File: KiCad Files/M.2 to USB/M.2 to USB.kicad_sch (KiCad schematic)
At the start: 32 parts, among them J1 M.2 A+E Key Connector, J2 Conn_2Rows-09Pins_ALT, U1 USB2422T_MJ, U2 AP2152SG-13, U3 MIC2876-5.0, U4 SN74LVC1G14DBVR, Y1 OSC24M-3.3I/S3

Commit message: New Renders and updated board
updated the footprints for usb2422, clock chip and m.2 connector.

made new 2D and 3D renders of updated board.
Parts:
- J1: now left out of the parts list
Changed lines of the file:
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@@
 		(unit 1)
 		(exclude_from_sim no)
-		(in_bom yes)
+		(in_bom no)
 		(on_board yes)
 		(dnp no)

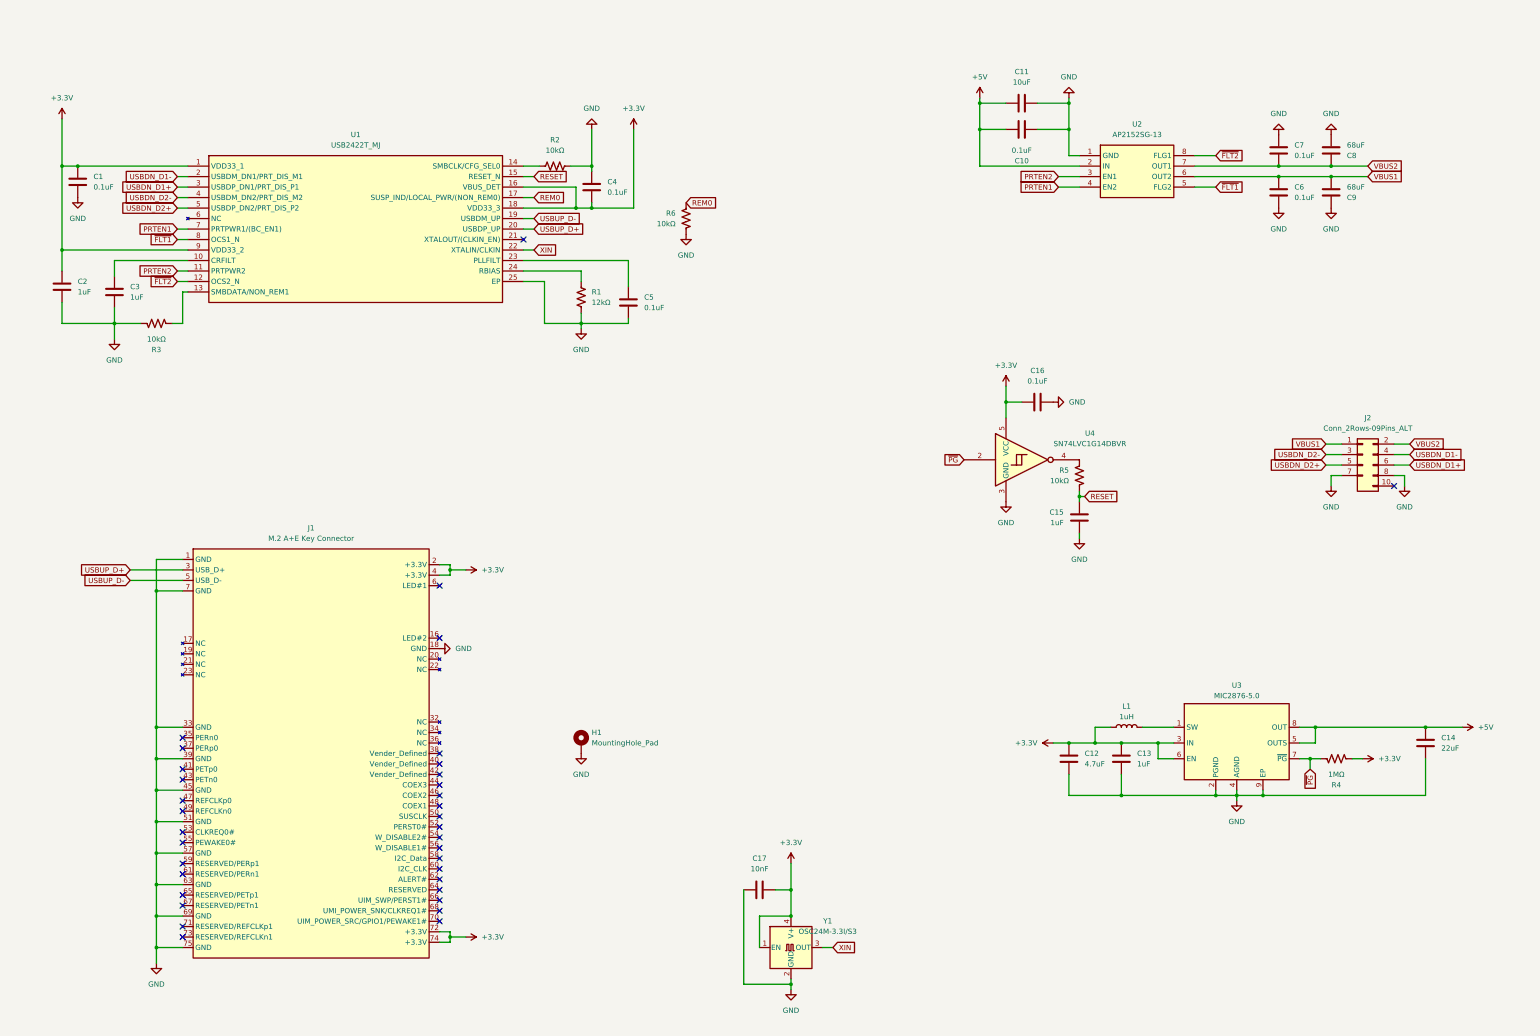
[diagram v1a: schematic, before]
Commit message: Updated v1.1 design
-updated v1.1 design
-finished schematic, pcb, render, gerber, and BOM
-removed old v1.0 files
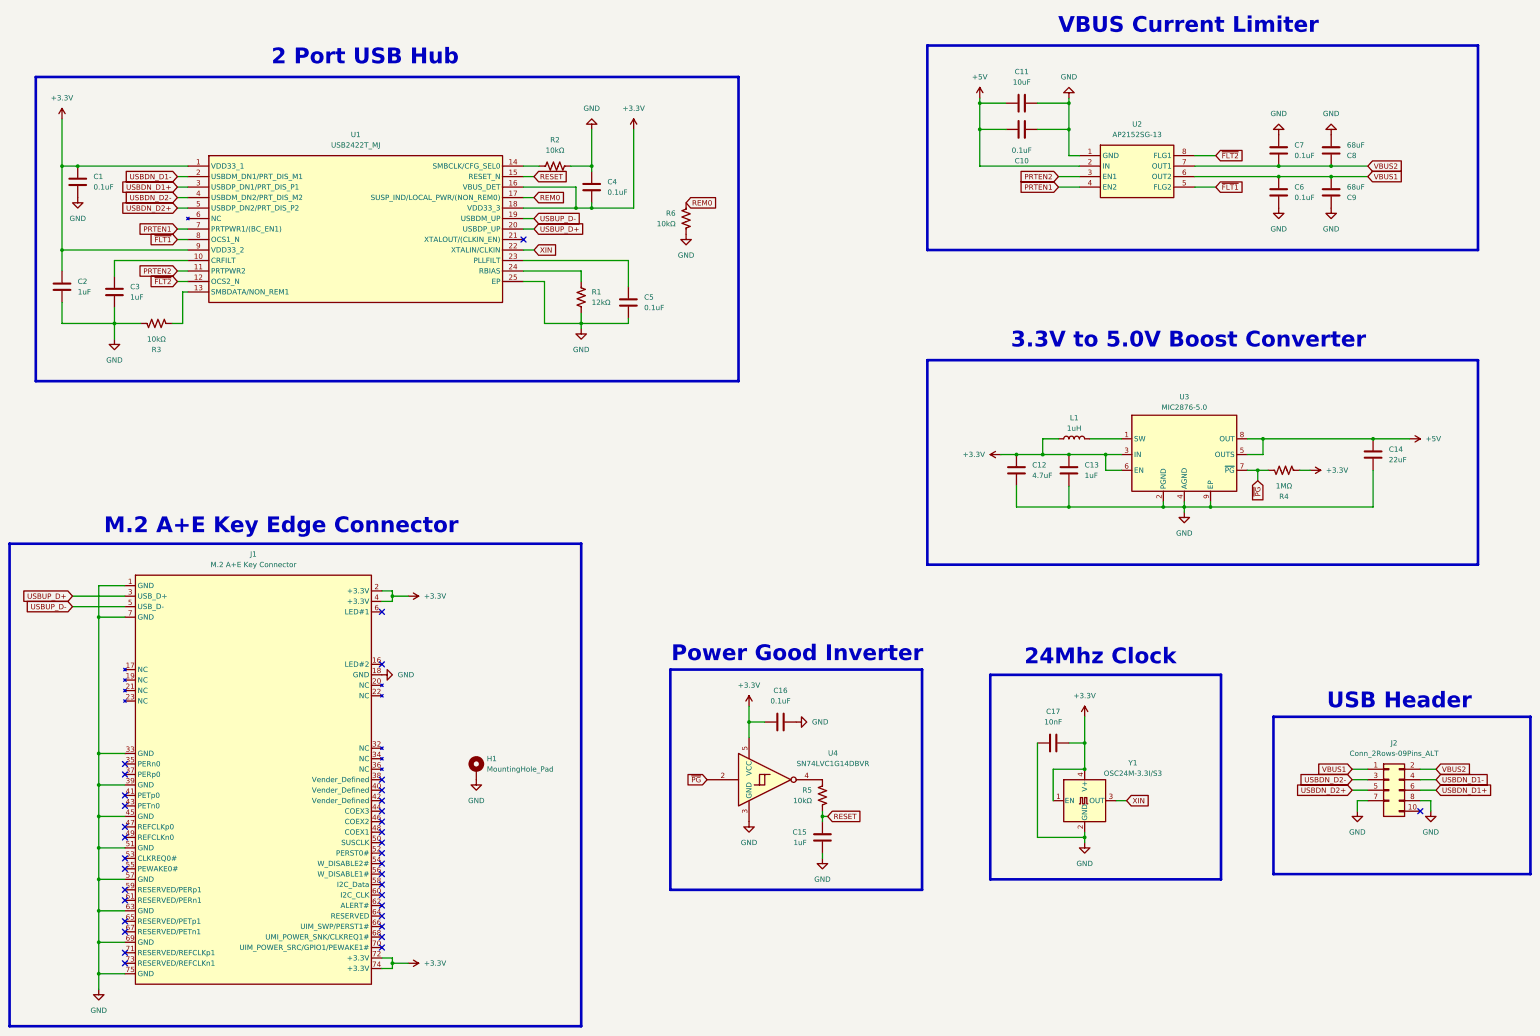
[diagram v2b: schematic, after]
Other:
- note added: "2 Port USB Hub"
- note added: "24Mhz Clock"
- note added: "3.3V to 5.0V Boost Converter"
- note added: "M.2 A+E Key Edge Connector"
- note added: "Power Good Inverter"
- note added: "USB Header"
- note added: "VBUS Current Limiter"
- title: (none) -> M.2 to USB 
- moved on the sheet: C12, C13, C14, C15, C16, C17, H1, J1, J2, L1, R4, R5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

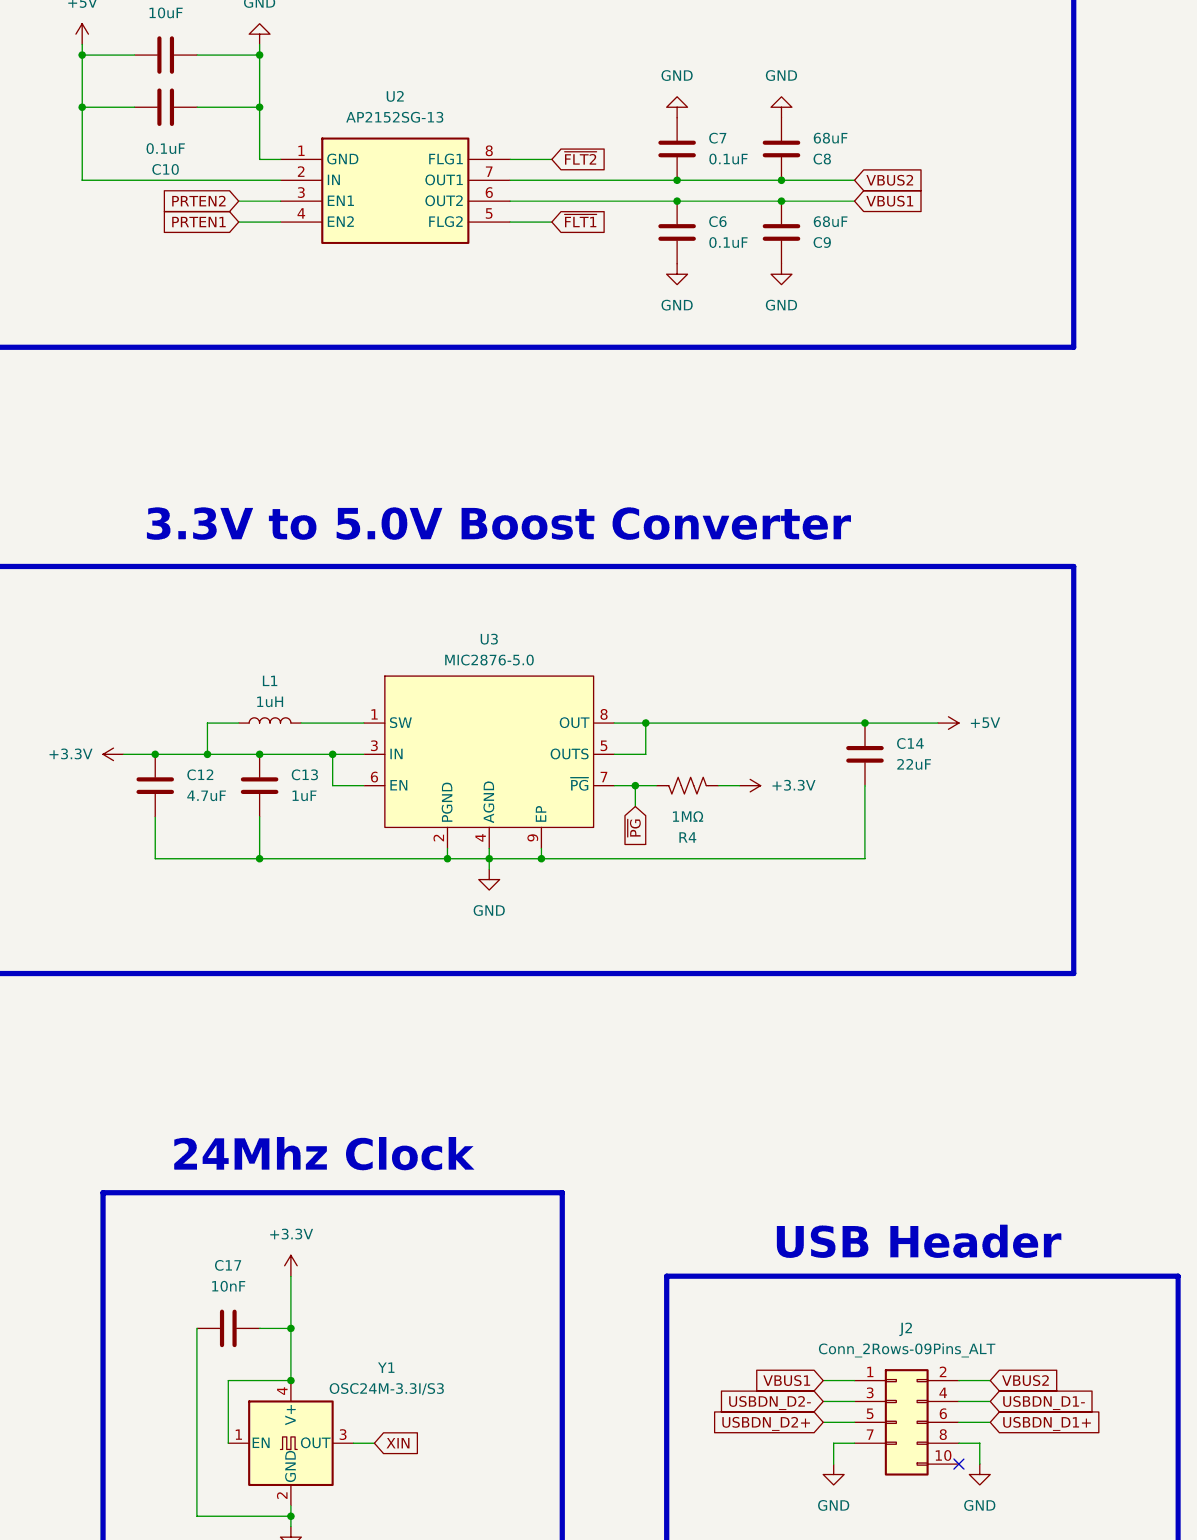
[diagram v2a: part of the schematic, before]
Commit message: fixed vbus nets
vbus nets were corrected so flt/en port from the hub lined up with the usb port on the header
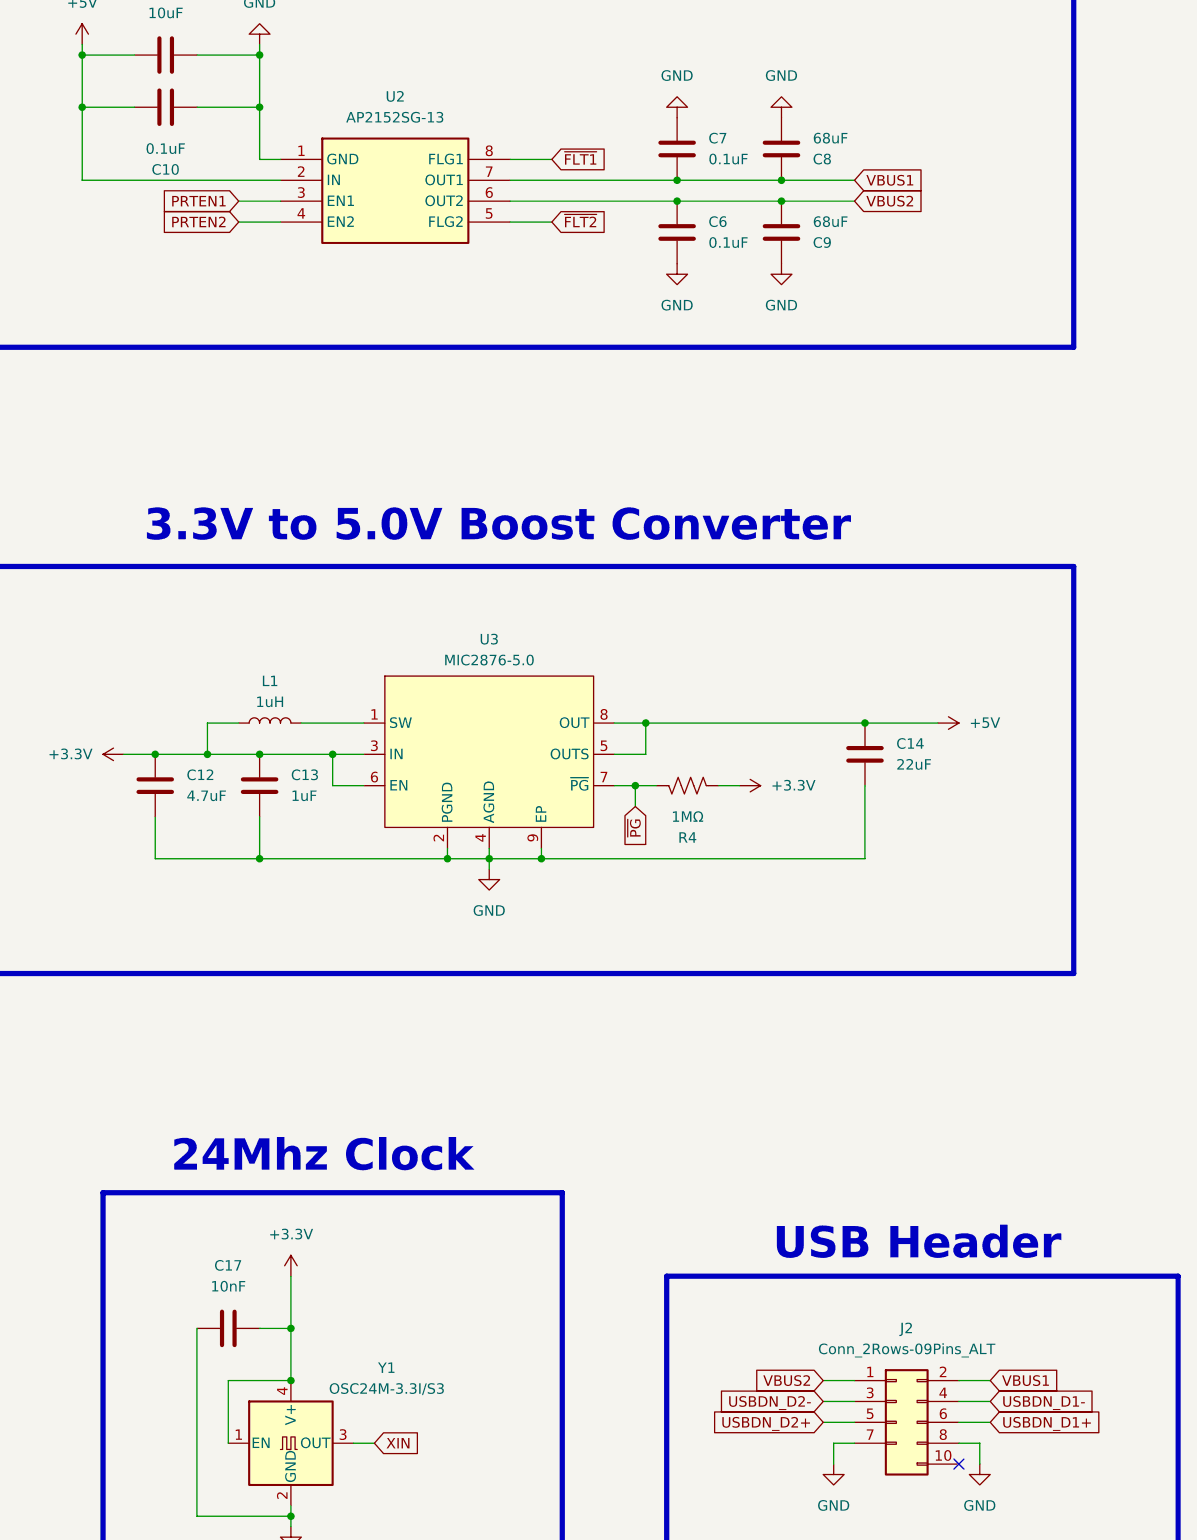
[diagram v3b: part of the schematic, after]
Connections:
- net PRTEN1: now also U2.3 (EN1); no longer U2.4 (EN2)
- net PRTEN2: now also U2.4 (EN2); no longer U2.3 (EN1)
- net VBUS1: now also C7.2, C8.1, J2.2 (Pin_2), U2.7 (OUT1); no longer C6.1, C9.2, J2.1 (Pin_1), U2.6 (OUT2)
- net VBUS2: now also C6.1, C9.2, J2.1 (Pin_1), U2.6 (OUT2); no longer C7.2, C8.1, J2.2 (Pin_2), U2.7 (OUT1)
- net ~{FLT1}: now also U2.8 (FLG1); no longer U2.5 (FLG2)
- net ~{FLT2}: now also U2.5 (FLG2); no longer U2.8 (FLG1)
